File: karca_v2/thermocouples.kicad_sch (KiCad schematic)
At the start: 17 parts, among them J7 Screw_Terminal_01x08

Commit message: updated
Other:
- moved on the sheet: D13, D14, D15, D16, D17, D19, D20, J7, TP10, TP11, TP12, TP13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

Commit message: Version alpha
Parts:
- removed D13, D14, D15, D16, D17, D18, D19, D20: D_Schottky, Diode_SMD:D_SMA, symbol Device:D_Schottky
- added C53, C73: 0.1u, Capacitor_SMD:C_1206_3216Metric, symbol Device:C
- added U12: NUP4202, Package_SO:TSOP-6_1.65x3.05mm_P0.95mm, symbol Power_Protection:NUP4202
- added U13: TLV9304xD, Package_SO:SO-14_3.9x8.65mm_P1.27mm, symbol Amplifier_Operational:TLV9304xD
- J8: renamed from J7; footprint (none) -> terminal blocks:P-2604-1108
- TP14: renamed from TP9; footprint (none) -> TestPoint:TestPoint_Pad_D2.0mm
- TP15: renamed from TP10; footprint (none) -> TestPoint:TestPoint_Pad_D2.0mm
- TP16: renamed from TP11; footprint (none) -> TestPoint:TestPoint_Pad_D2.0mm
- TP17: renamed from TP12; footprint (none) -> TestPoint:TestPoint_Pad_D2.0mm
- TP18: renamed from TP13; footprint (none) -> TestPoint:TestPoint_Pad_D2.0mm
- TP19: renamed from TP14; footprint (none) -> TestPoint:TestPoint_Pad_D2.0mm
- TP20: renamed from TP15; footprint (none) -> TestPoint:TestPoint_Pad_D2.0mm
- TP21: renamed from TP16; footprint (none) -> TestPoint:TestPoint_Pad_D2.0mm
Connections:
- net +5V: now also C53.2, U12.5, U13.4 (V+)
- net GND: now also C53.1, C73.1, C73.2, U12.2, U13.11 (V-)
- net TC_1: now also U12.6
- net TC_2: now also U12.4
- net TC_3: now also U12.3
- net TC_4: now also U12.1
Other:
- moved on the sheet: J8, TP14, TP15, TP16, TP17, TP18, TP19, TP20, TP21

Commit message: fkkkkkkkkkk
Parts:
- U10: renamed from U12; footprint Package_SO:TSOP-6_1.65x3.05mm_P0.95mm -> Package_TO_SOT_SMD:SOT-363_SC-70-6
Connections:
- net TC_1: now also U10.1; no longer U10.6
- net TC_2: now also U10.3; no longer U10.4
- net TC_3: now also U10.4; no longer U10.3
- net TC_4: now also U10.6; no longer U10.1
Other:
- moved on the sheet: TP14, TP15, TP16, TP17, U10

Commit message: discrete traces
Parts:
- renumbered C53 to C16, C73 to C17, TP21 to TP20, TP20 to TP21, U10 to U12
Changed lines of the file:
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@@
   (symbol (lib_id "power:+5V") (at 182.88 107.95 0) (unit 1)
     (in_bom yes) (on_board yes) (dnp no) (fields_autoplaced)
-    (property "Reference" "#PWR047" (at 182.88 111.76 0)
+    (property "Reference" "#PWR057" (at 182.88 111.76 0)
       (effects (font (size 1.27 1.27)) hide)
     )
@@
       (project "karca_v2"
         (path "/29cf4797-56f2-4f57-ae95-7df639362e3c/4e6489a2-f37d-4c34-b99f-d7711dd1a6f1"
-          (reference "#PWR047") (unit 1)
+          (reference "#PWR057") (unit 1)
         )
       )
@@
   (symbol (lib_id "power:GND") (at 60.96 156.718 0) (unit 1)
     (in_bom yes) (on_board yes) (dnp no) (fields_autoplaced)
-    (property "Reference" "#PWR050" (at 60.96 163.068 0)
+    (property "Reference" "#PWR060" (at 60.96 163.068 0)
       (effects (font (size 1.27 1.27)) hide)
     )
@@
       (project "karca_v2"
         (path "/29cf4797-56f2-4f57-ae95-7df639362e3c/4e6489a2-f37d-4c34-b99f-d7711dd1a6f1"
-          (reference "#PWR050") (unit 1)
+          (reference "#PWR060") (unit 1)
         )
       )
@@
   (symbol (lib_id "Connector:TestPoint") (at 192.532 160.782 0) (unit 1)
     (in_bom yes) (on_board yes) (dnp no)
-    (property "Reference" "TP21" (at 187.452 151.892 0)
+    (property "Reference" "TP20" (at 187.452 151.892 0)
       (effects (font (size 1.27 1.27)) (justify left))
     )
@@
       (project "karca_v2"
         (path "/29cf4797-56f2-4f57-ae95-7df639362e3c/4e6489a2-f37d-4c34-b99f-d7711dd1a6f1"
-          (reference "TP21") (unit 1)
+          (reference "TP20") (unit 1)
         )
       )
@@
   (symbol (lib_id "power:GND") (at 52.705 163.195 0) (unit 1)
     (in_bom yes) (on_board yes) (dnp no) (fields_autoplaced)
-    (property "Reference" "#PWR0154" (at 52.705 169.545 0)
+    (property "Reference" "#PWR061" (at 52.705 169.545 0)
       (effects (font (size 1.27 1.27)) hide)
     )
@@
       (project "karca_v2"
         (path "/29cf4797-56f2-4f57-ae95-7df639362e3c/4e6489a2-f37d-4c34-b99f-d7711dd1a6f1"
-          (reference "#PWR0154") (unit 1)
+          (reference "#PWR061") (unit 1)
         )
       )
@@
   (symbol (lib_id "power:+5V") (at 60.96 138.811 0) (unit 1)
     (in_bom yes) (on_board yes) (dnp no) (fields_autoplaced)
-    (property "Reference" "#PWR049" (at 60.96 142.621 0)
+    (property "Reference" "#PWR058" (at 60.96 142.621 0)
       (effects (font (size 1.27 1.27)) hide)
     )
@@
       (project "karca_v2"
         (path "/29cf4797-56f2-4f57-ae95-7df639362e3c/4e6489a2-f37d-4c34-b99f-d7711dd1a6f1"
-          (reference "#PWR049") (unit 1)
+          (reference "#PWR058") (unit 1)
         )
       )
@@
   (symbol (lib_id "Device:C") (at 52.705 142.875 180) (unit 1)
     (in_bom yes) (on_board yes) (dnp no)
-    (property "Reference" "C53" (at 47.625 140.335 0)
+    (property "Reference" "C16" (at 47.625 140.335 0)
       (effects (font (size 1.27 1.27)) (justify right))
     )
@@
       (project "karca_v2"
         (path "/29cf4797-56f2-4f57-ae95-7df639362e3c/4e6489a2-f37d-4c34-b99f-d7711dd1a6f1"
-          (reference "C53") (unit 1)
+          (reference "C16") (unit 1)
         )
       )
@@
   (symbol (lib_id "Connector:TestPoint") (at 160.655 161.925 0) (unit 1)
     (in_bom yes) (on_board yes) (dnp no)
-    (property "Reference" "TP20" (at 158.115 154.305 0)
+    (property "Reference" "TP21" (at 158.115 154.305 0)
       (effects (font (size 1.27 1.27)) (justify left))
     )
@@
       (project "karca_v2"
         (path "/29cf4797-56f2-4f57-ae95-7df639362e3c/4e6489a2-f37d-4c34-b99f-d7711dd1a6f1"
-          (reference "TP20") (unit 1)
+          (reference "TP21") (unit 1)
         )
       )
@@
   (symbol (lib_id "Power_Protection:NUP4202") (at 173.99 106.045 180) (unit 1)
     (in_bom yes) (on_board yes) (dnp no)
-    (property "Reference" "U10" (at 170.18 113.665 0)
+    (property "Reference" "U12" (at 170.18 113.665 0)
       (effects (font (size 1.27 1.27)) (justify left))
     )
@@
       (project "karca_v2"
         (path "/29cf4797-56f2-4f57-ae95-7df639362e3c/4e6489a2-f37d-4c34-b99f-d7711dd1a6f1"
-          (reference "U10") (unit 1)
+          (reference "U12") (unit 1)
         )
       )
@@
   (symbol (lib_id "Device:C") (at 52.705 159.385 180) (unit 1)
     (in_bom yes) (on_board yes) (dnp no)
-    (property "Reference" "C73" (at 47.625 156.845 0)
+    (property "Reference" "C17" (at 47.625 156.845 0)
       (effects (font (size 1.27 1.27)) (justify right))
     )
@@
       (project "karca_v2"
         (path "/29cf4797-56f2-4f57-ae95-7df639362e3c/4e6489a2-f37d-4c34-b99f-d7711dd1a6f1"
-          (reference "C73") (unit 1)
+          (reference "C17") (unit 1)
         )
       )
@@
   (symbol (lib_id "power:GND") (at 183.515 97.155 0) (unit 1)
     (in_bom yes) (on_board yes) (dnp no)
-    (property "Reference" "#PWR048" (at 183.515 103.505 0)
+    (property "Reference" "#PWR056" (at 183.515 103.505 0)
       (effects (font (size 1.27 1.27)) hide)
     )
@@
       (project "karca_v2"
         (path "/29cf4797-56f2-4f57-ae95-7df639362e3c/4e6489a2-f37d-4c34-b99f-d7711dd1a6f1"
-          (reference "#PWR048") (unit 1)
+          (reference "#PWR056") (unit 1)
         )
       )
@@
   (symbol (lib_id "power:GND") (at 52.705 146.685 0) (unit 1)
     (in_bom yes) (on_board yes) (dnp no) (fields_autoplaced)
-    (property "Reference" "#PWR0155" (at 52.705 153.035 0)
+    (property "Reference" "#PWR059" (at 52.705 153.035 0)
       (effects (font (size 1.27 1.27)) hide)
     )
@@
       (project "karca_v2"
         (path "/29cf4797-56f2-4f57-ae95-7df639362e3c/4e6489a2-f37d-4c34-b99f-d7711dd1a6f1"
-          (reference "#PWR0155") (unit 1)
-        )
-      )
+          (reference "#PWR059") (unit 1)
+        )
+      )

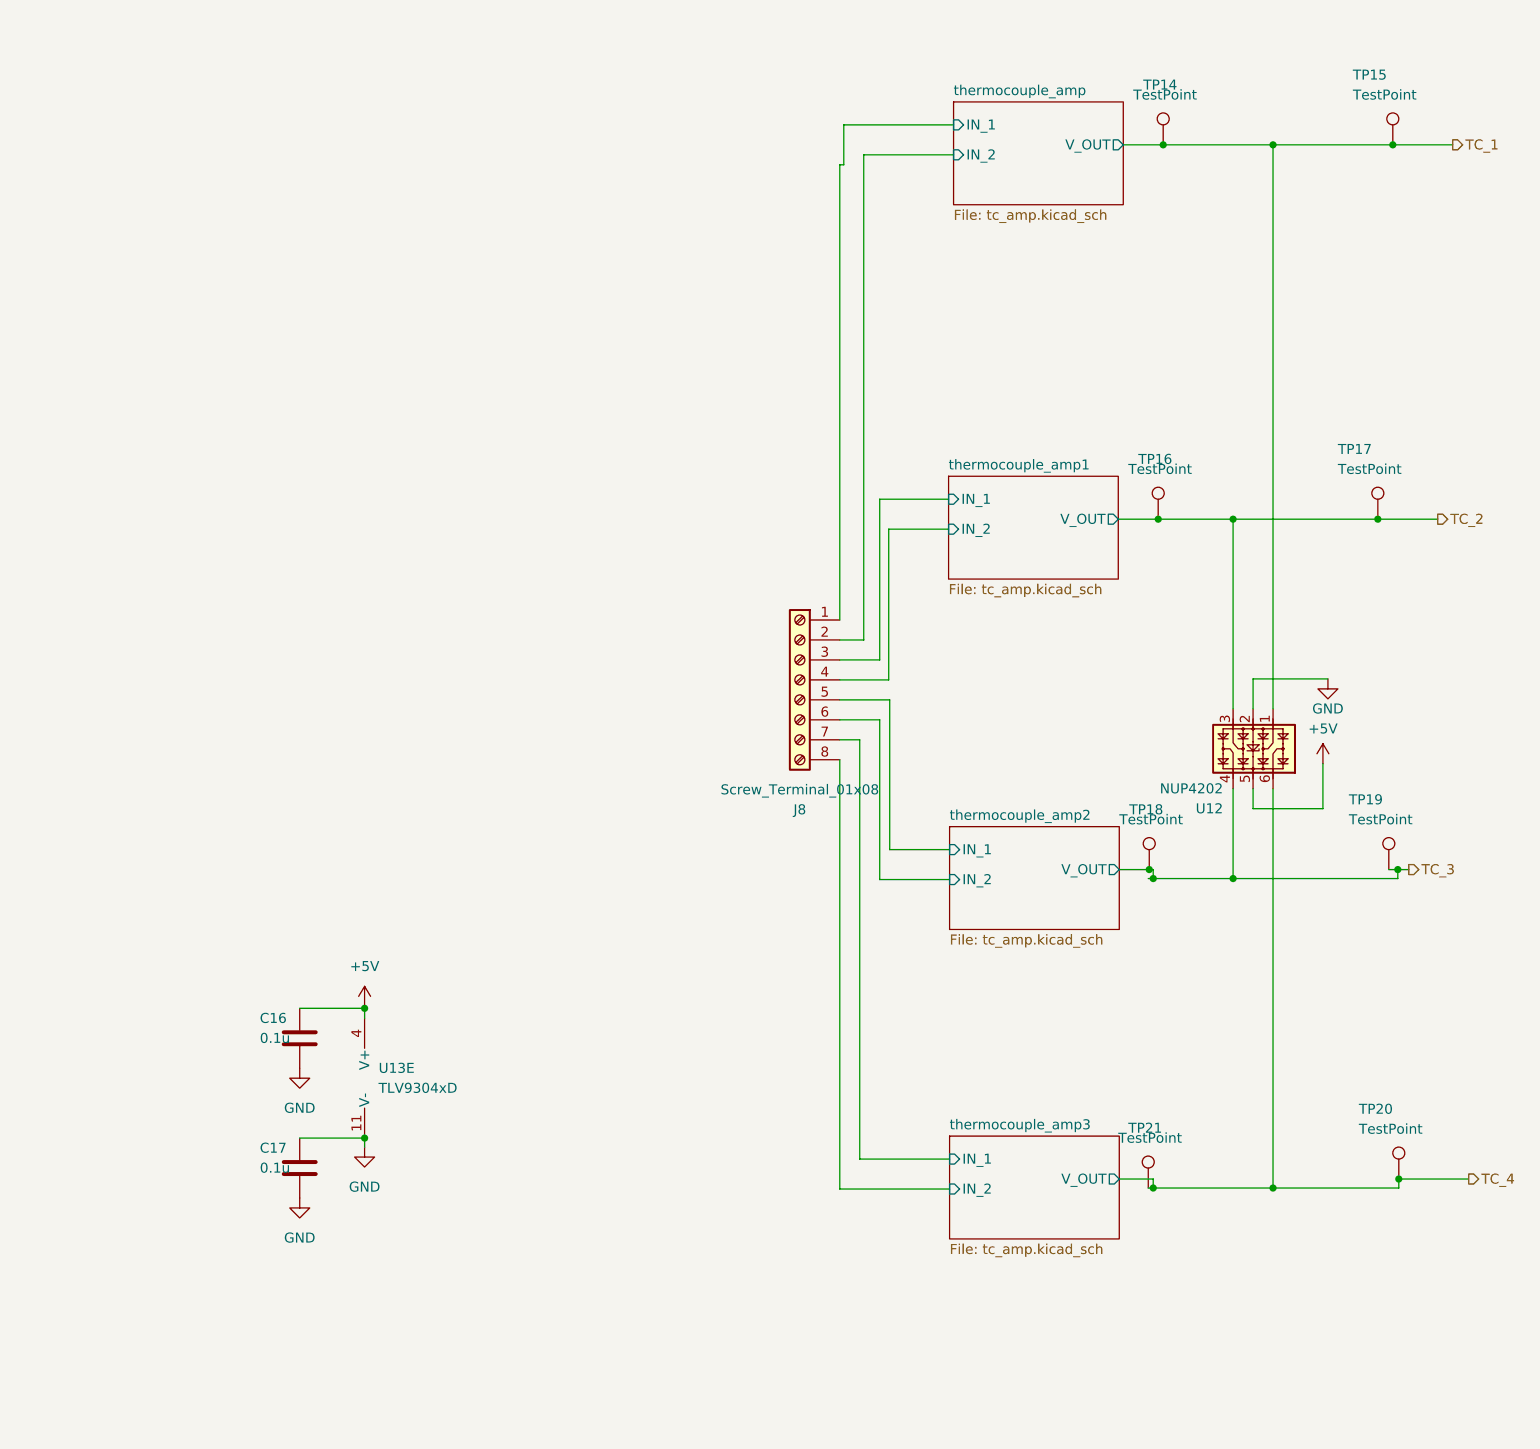
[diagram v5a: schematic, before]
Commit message: fixed TVS Diodes
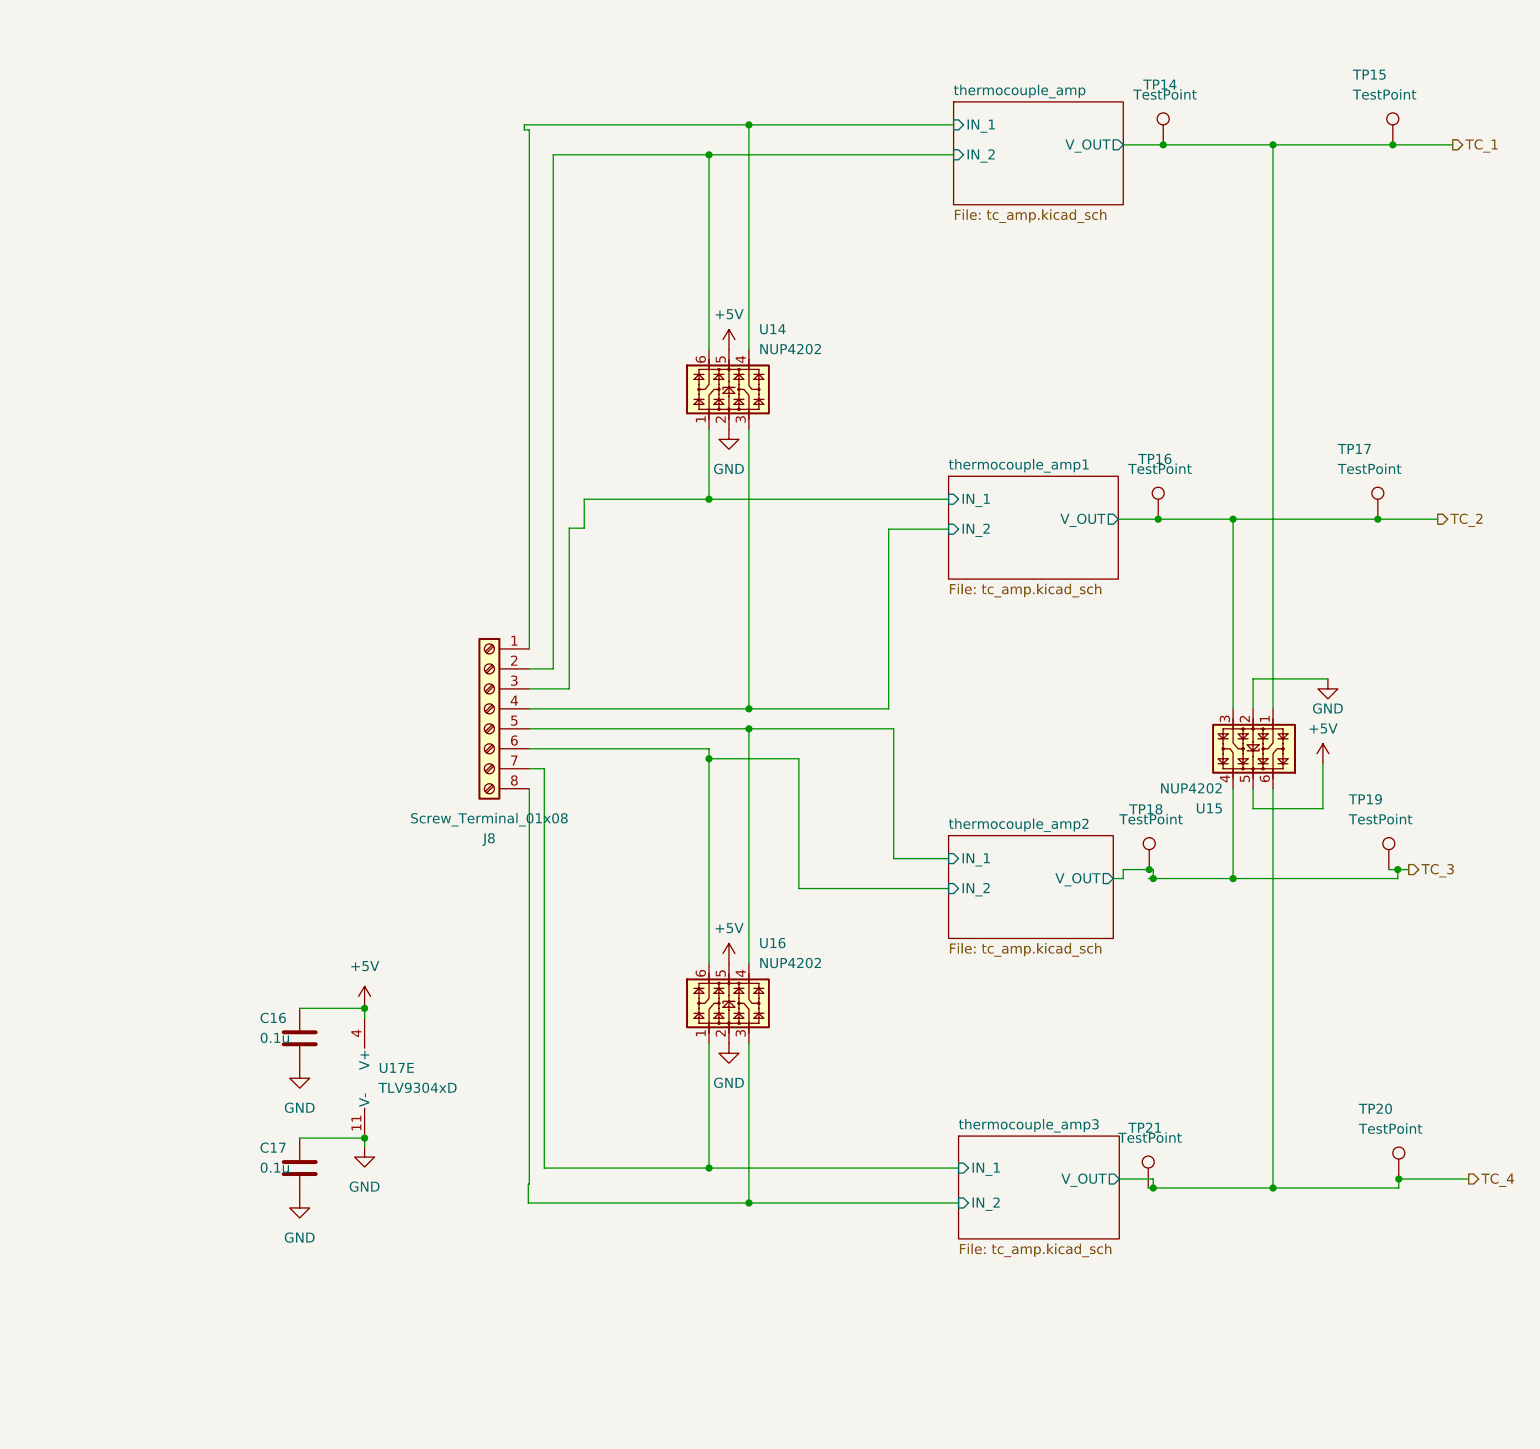
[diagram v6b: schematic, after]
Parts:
- added U14, U16: NUP4202, Package_TO_SOT_SMD:SOT-363_SC-70-6, symbol Power_Protection:NUP4202
- renumbered U12 to U15, U13 to U17
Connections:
- net +5V: now also U14.5, U16.5
- net GND: now also U14.2, U16.2
- net thermocouple_amp/IN_1: now also U14.4
- net thermocouple_amp/IN_2: now also U14.6
- net thermocouple_amp1/IN_1: now also U14.1
- net thermocouple_amp1/IN_2: now also U14.3
- net thermocouple_amp2/IN_1: now also U16.4
- net thermocouple_amp2/IN_2: now also U16.6
- net thermocouple_amp3/IN_1: now also U16.1
- net thermocouple_amp3/IN_2: now also U16.3
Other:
- moved on the sheet: J8

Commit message: Fixed ground capacitors
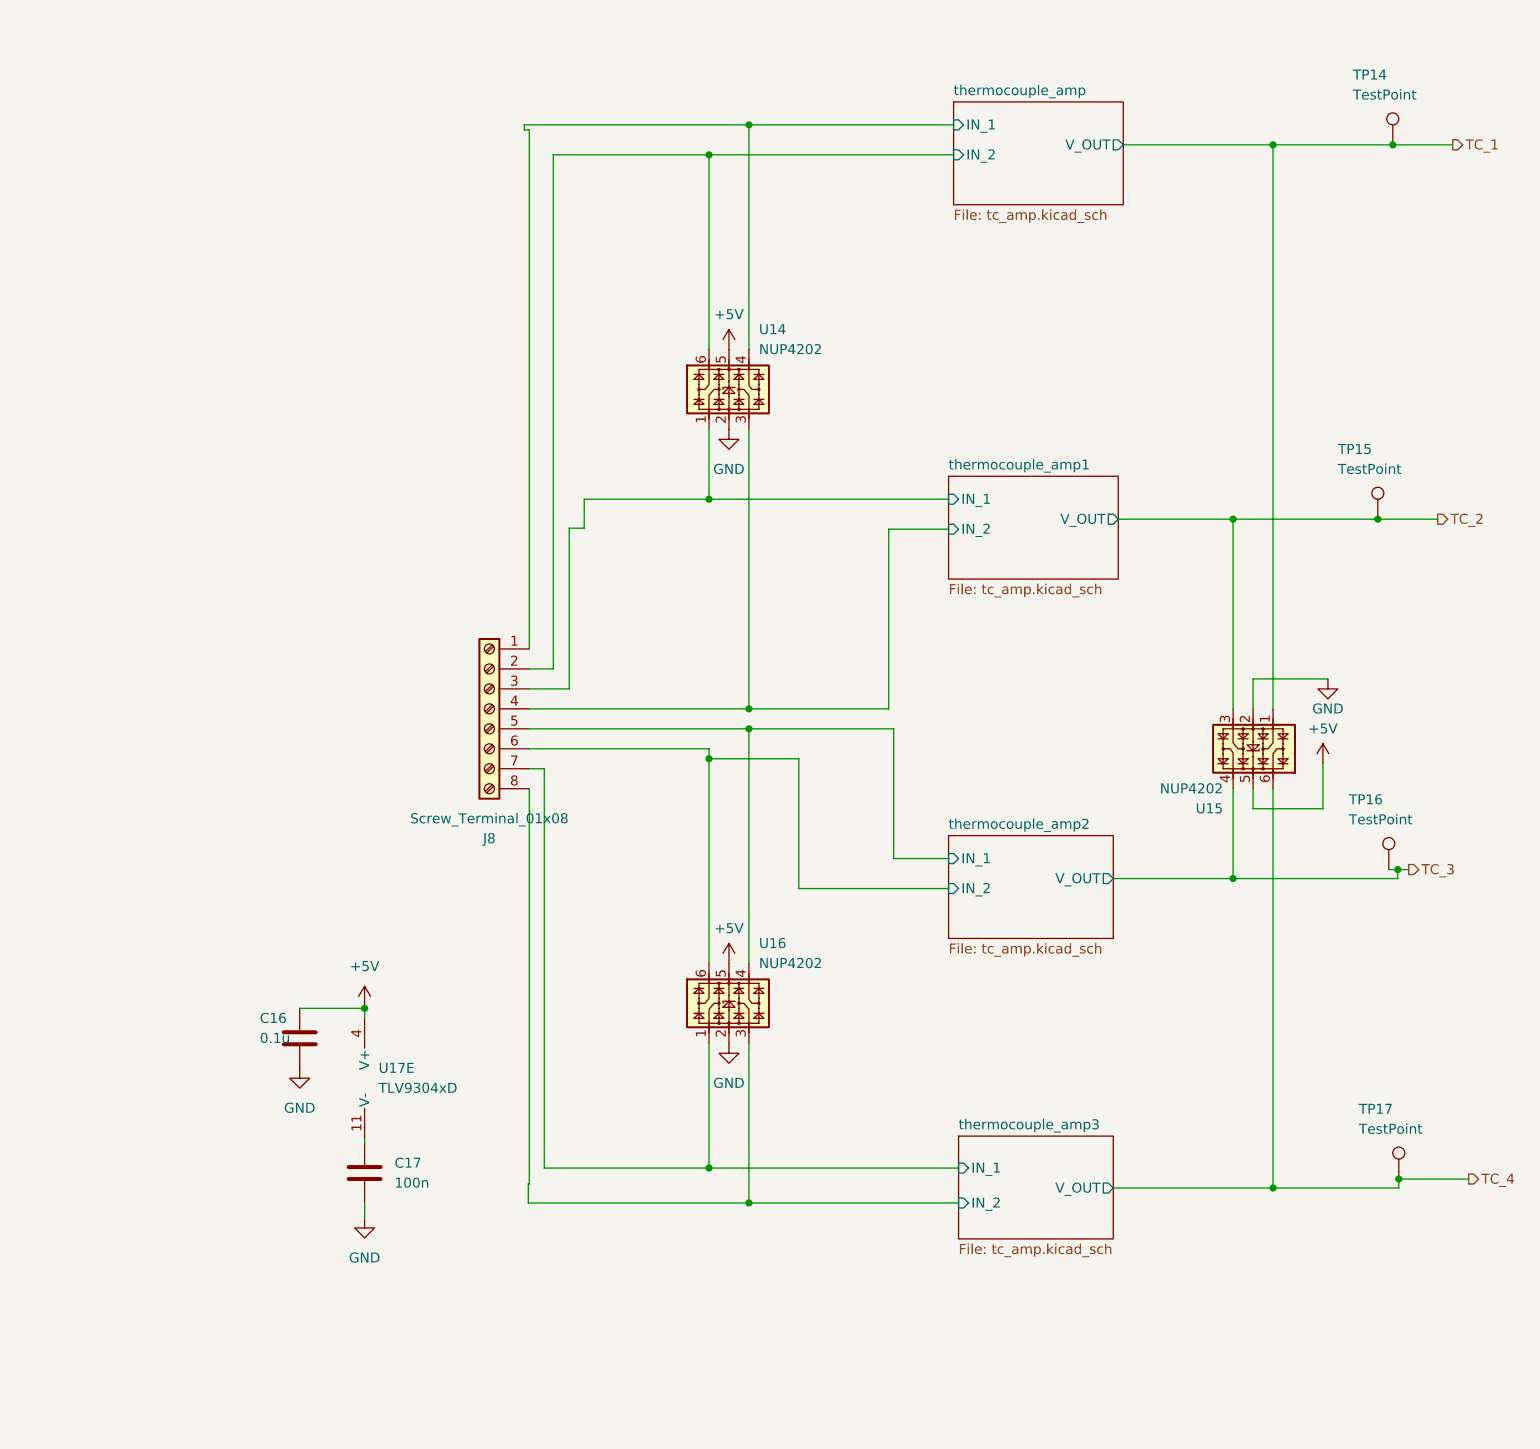
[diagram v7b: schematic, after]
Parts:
- removed TP14, TP16, TP18, TP21: TestPoint, TestPoint:TestPoint_Pad_D2.0mm, symbol Connector:TestPoint
- C17: value 0.1u -> 100n
- renumbered TP15 to TP14, TP17 to TP15, TP19 to TP16, TP20 to TP17
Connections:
- net GND: no longer C17.2, U17.11 (V-)
- new net: C17.2, U17.11 (V-)
